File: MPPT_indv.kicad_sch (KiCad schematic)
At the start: 24 parts, among them Q8 Q_NMOS, Q9 Q_NMOS, U15 LTC4162IUFD-LADM_PBF

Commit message: Started layout of the Ideal diode input (LTC4417)
I'm considering getting rid of the second 3V3 buck but will need to weigh the pros and cons a little more before commiting
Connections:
- net VOUT_+X renamed VOUT
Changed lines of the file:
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@@
 	(wire
 		(pts
-			(xy 100.33 99.06) (xy 110.49 99.06)
+			(xy 105.41 99.06) (xy 110.49 99.06)
 		)
 		(stroke
@@
 		)
 	)
-	(label "VOUT_+X"
-		(at 203.2 78.74 180)
-		(effects
-			(font
-				(size 1.27 1.27)
-			)
-			(justify right bottom)
-		)
-	)
 	(label "VCC2P5_+X"
 		(at 173.99 73.66 180)
@@
 		)
 	)
-	(label "VOUT_+X"
-		(at 100.33 99.06 0)
-		(effects
-			(font
-				(size 1.27 1.27)
-			)
-			(justify left bottom)
-		)
-	)
 	(hierarchical_label "SDA"
 		(shape input)
@@
 			)
 			(justify right)
+		)
+	)
+	(hierarchical_label "VOUT"
+		(shape input)
+		(at 203.2 78.74 0)
+		(effects
+			(font
+				(size 1.27 1.27)
+			)
+			(justify left)
 		)
 	)
@@
 		)
 	)
+	(hierarchical_label "VOUT"
+		(shape input)
+		(at 105.41 99.06 180)
+		(effects
+			(font
+				(size 1.27 1.27)
+			)
+			(justify right)
+		)
+	)

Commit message: Efuses for this board and Battery board
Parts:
- renumbered C57 to C64, C58 to C65, C59 to C66, C60 to C67, C61 to C68, C62 to C69, C63 to C70, C64 to C71, C65 to C72, C66 to C73, C67 to C74, D6 to D10, L4 to L3, R78 to R73, R79 to R74, R80 to R75, R81 to R76, R82 to R77, R83 to R78, R84 to R79, R85 to R80

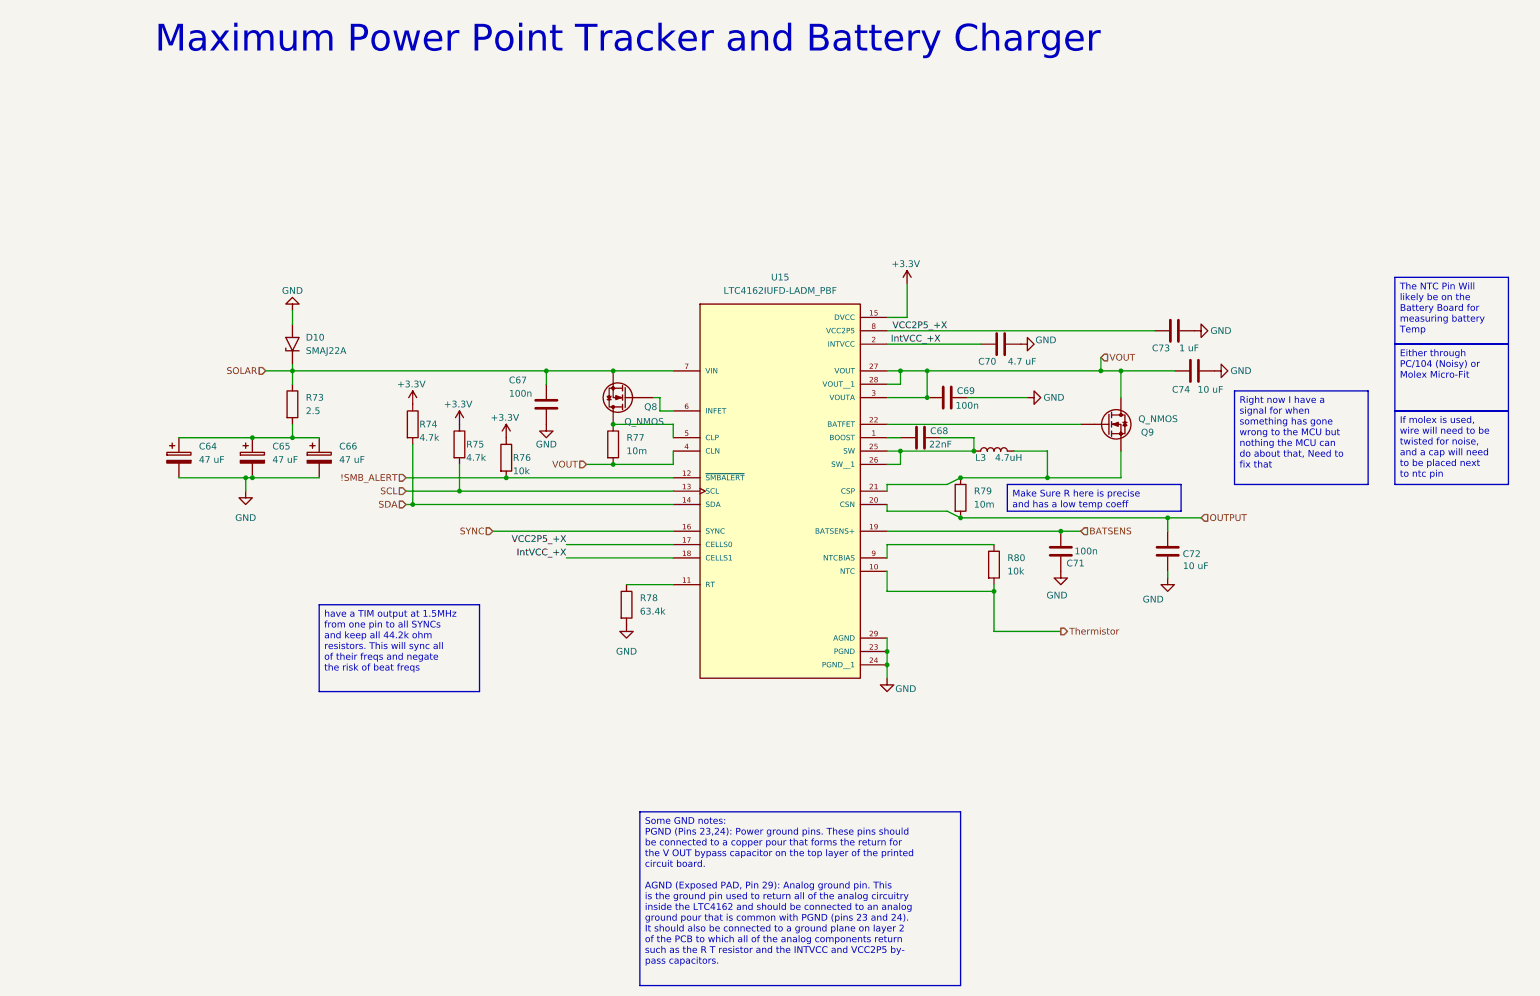
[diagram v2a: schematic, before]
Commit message: Added Batt 1 and Batt 2 charging
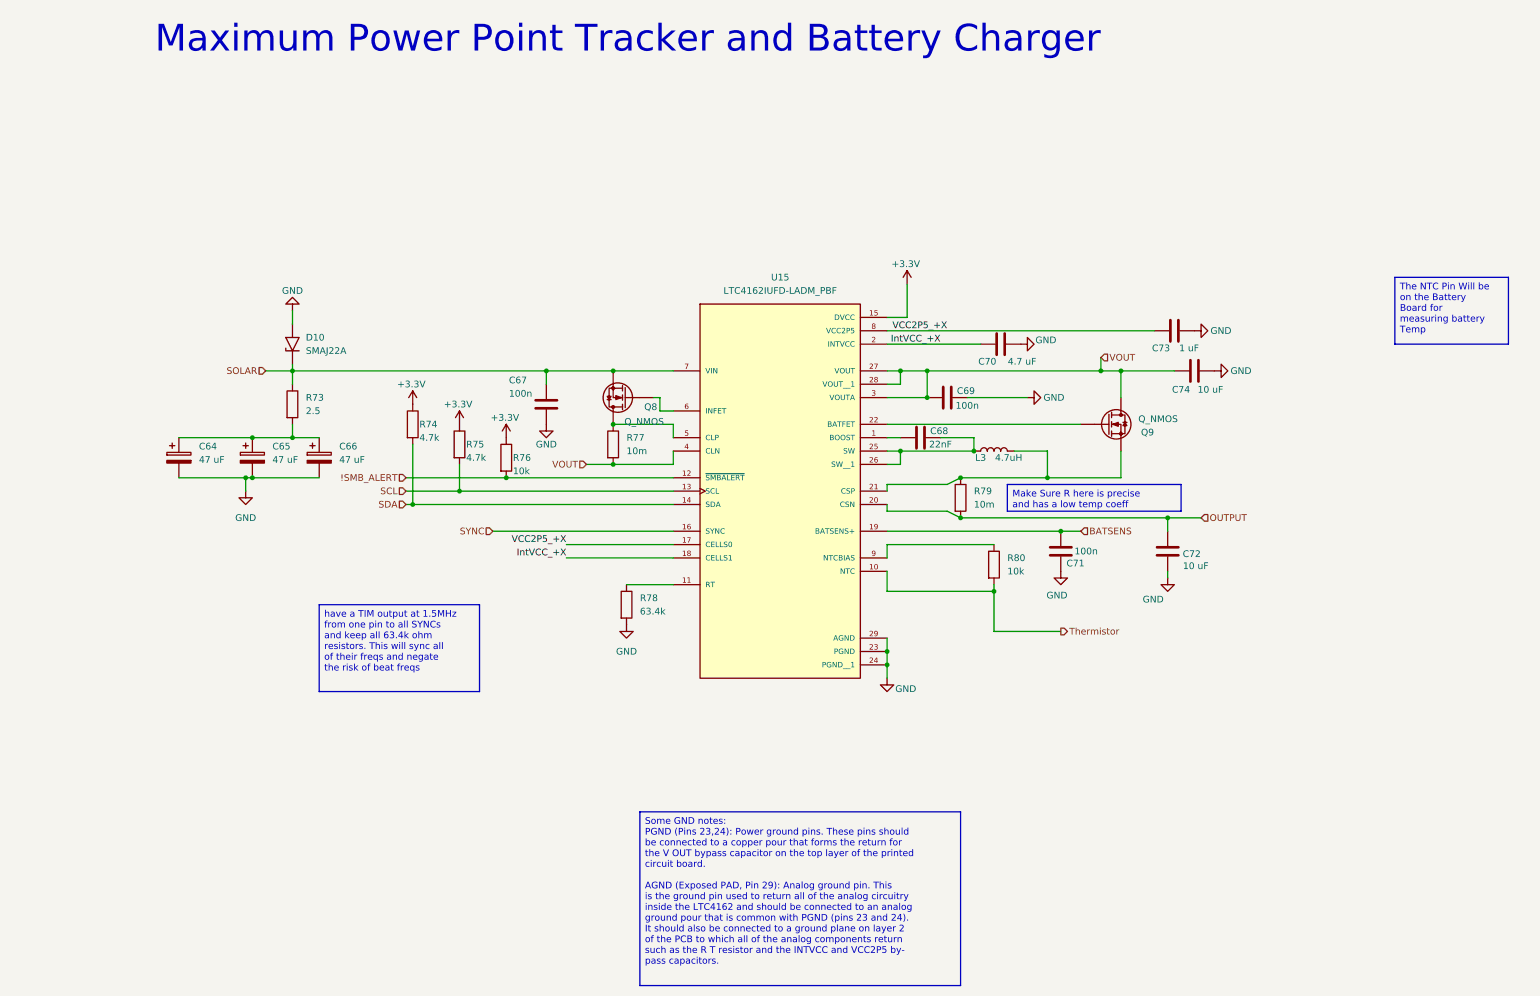
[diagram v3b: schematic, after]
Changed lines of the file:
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@@
 		)
 	)
-	(text_box "The NTC Pin Will likely be on the Battery Board for measuring battery Temp"
+	(text_box "The NTC Pin Will be on the Battery Board for measuring battery Temp"
 		(exclude_from_sim no)
 		(at 259.08 63.5 0)
@@
 		)
 	)
-	(text_box "Either through PC/104 (Noisy) or Molex Micro-Fit"
-		(exclude_from_sim no)
-		(at 259.08 76.2 0)
-		(size 21.59 12.7)
-		(margins 0.9525 0.9525 0.9525 0.9525)
-		(stroke
-			(width 0)
-			(type solid)
-		)
-		(fill
-			(type color)
-			(color 158 218 255 1)
-		)
-		(effects
-			(font
-				(size 1.27 1.27)
-			)
-			(justify left top)
-		)
-	)
-	(text_box "have a TIM output at 1.5MHz from one pin to all SYNCs and keep all 44.2k ohm resistors. This will sync all of their freqs and negate the risk of beat freqs"
+	(text_box "have a TIM output at 1.5MHz from one pin to all SYNCs and keep all 63.4k ohm resistors. This will sync all of their freqs and negate the risk of beat freqs"
 		(exclude_from_sim no)
 		(at 54.61 125.73 0)
@@
 		(margins 0.9525 0.9525 0.9525 0.9525)
 		(stroke
-			(width 0)
-			(type solid)
-		)
-		(fill
-			(type color)
-			(color 158 218 255 1)
-		)
-		(effects
-			(font
-				(size 1.27 1.27)
-			)
-			(justify left top)
-		)
-	)
-	(text_box "If molex is used, wire will need to be twisted for noise, and a cap will need to be placed next to ntc pin\n"
-		(exclude_from_sim no)
-		(at 259.08 88.9 0)
-		(size 21.59 13.97)
-		(margins 0.9525 0.9525 0.9525 0.9525)
-		(stroke
-			(width 0)
-			(type solid)
-		)
-		(fill
-			(type color)
-			(color 158 218 255 1)
-		)
-		(effects
-			(font
-				(size 1.27 1.27)
-			)
-			(justify left top)
-		)
-	)
-	(text_box "Right now I have a signal for when something has gone wrong to the MCU but nothing the MCU can do about that, Need to fix that"
-		(exclude_from_sim no)
-		(at 228.6 85.09 0)
-		(size 25.4 17.78)
-		(margins 0.9525 0.9525 0.9525 0.9525)
-		(stroke
